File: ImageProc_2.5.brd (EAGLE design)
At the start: 49.8 x 23.2 mm, 117 parts, among them IC1 XC61GC3002HR-G, IC10 AT45DB642D-CNU, IC2 MIC5335-SPYMT, IC3 MIC5335-JGYMT, IC4 DSPIC33FJ128MC706A, IC5 AT86RF233-ZU, IC6 LTC6088, IC7 DRV8833RTY, IC8 DRV8833RTY, IC9 MPU-6000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

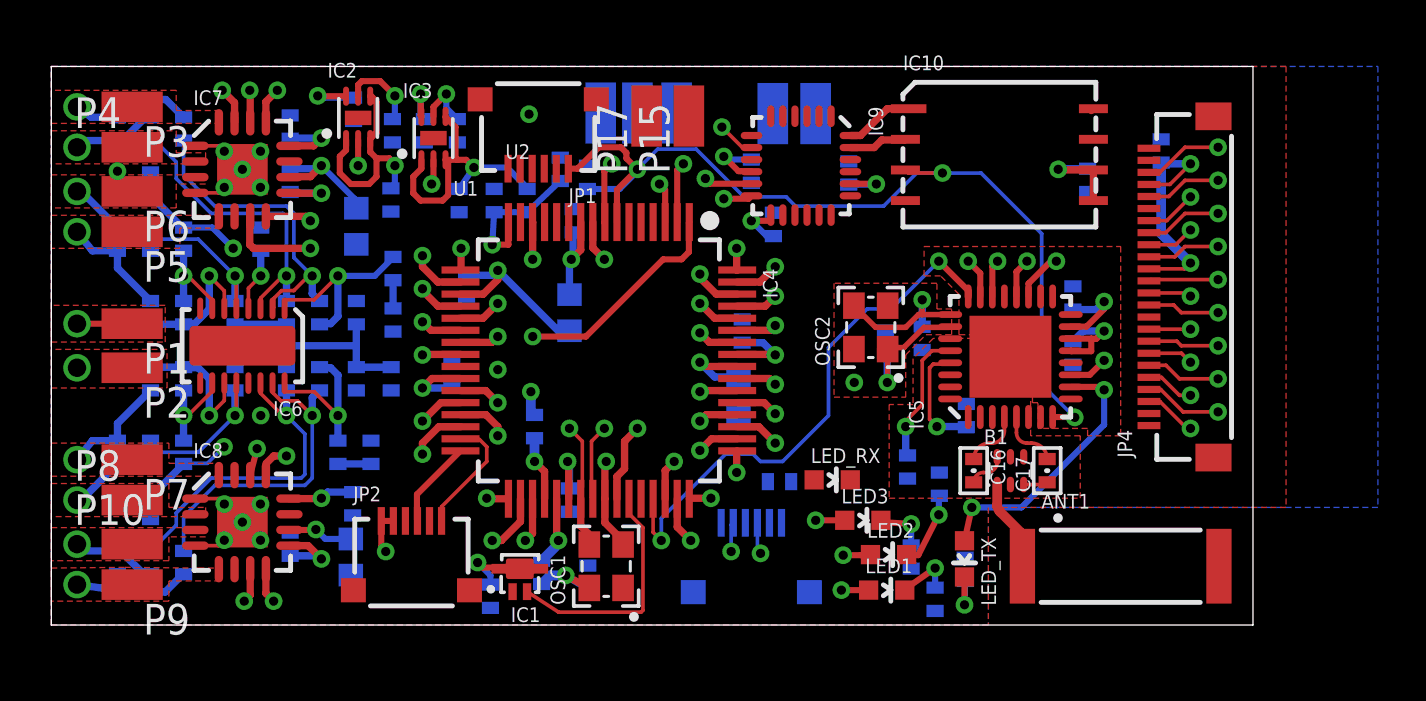
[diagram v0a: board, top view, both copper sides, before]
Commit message: ran DRC, fixed DRC issues for top and ground.
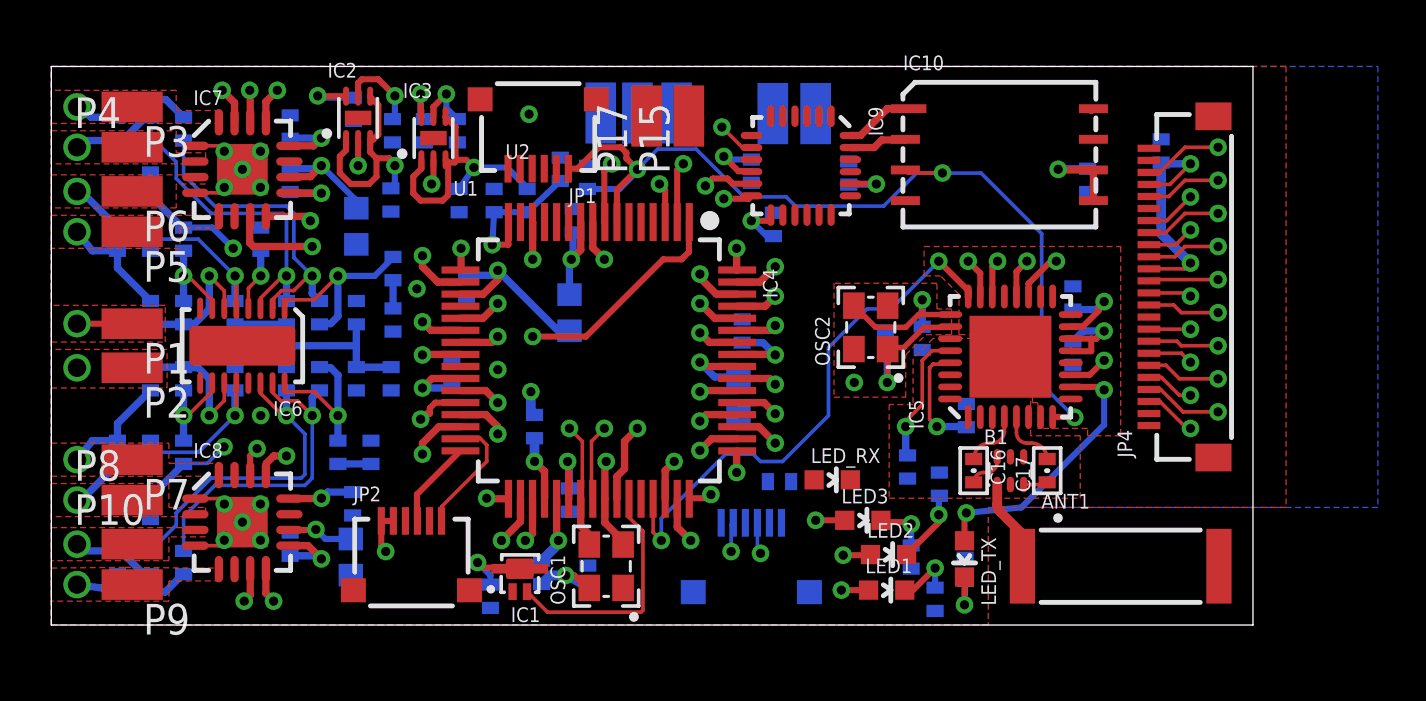
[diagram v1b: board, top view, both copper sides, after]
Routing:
- net CAM_HREF: track 39.2 -> 35.6 mm
- net SCL1: track 57.9 -> 55.7 mm
- net GND: track 14.9 -> 13.0 mm, vias 20 -> 19
- net SDI1: track 31.6 -> 31.1 mm

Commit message: Fixed rest of the initial DRC errors.
Down to 24 air wires.

Having to be creative for the pads.
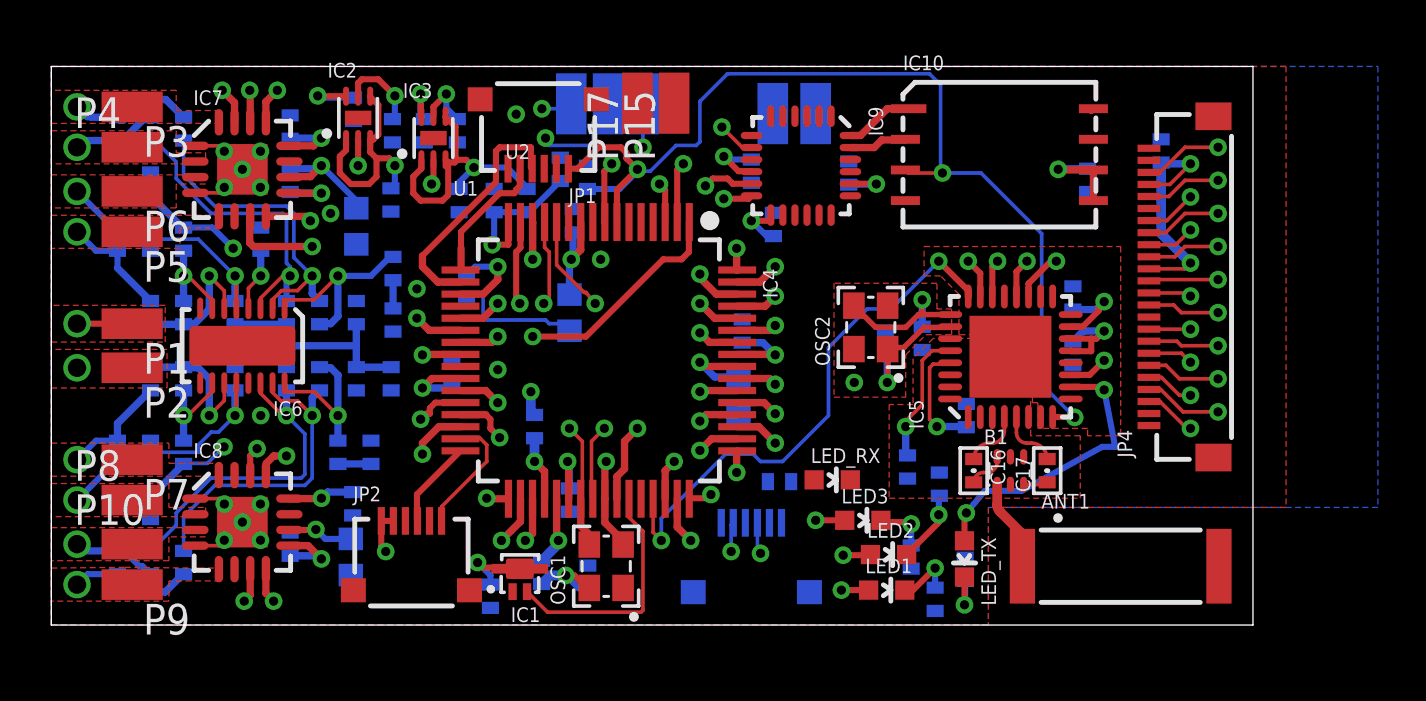
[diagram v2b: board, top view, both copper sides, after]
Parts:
- moved P13 1.42 mm to (24.6, 21.6)
- moved P11 1.28 mm to (21.6, 21.6)
- moved P12 1.28 mm to (23.1, 21.6)
- moved P15 0.81 mm to (25.8, 21.6)
- moved P17 0.66 mm to (24.3, 21.6)
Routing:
- net MOTOR_C_IN2: track 2.41 -> 41.7 mm, vias 2 -> 3
- net AN3/INDX/RB3: track 0.00 -> 21.3 mm, vias 0 -> 2
- net MOTOR_B_IN1: track 5.60 -> 26.3 mm
- net AN1/RB1: track 0.00 -> 17.8 mm, vias 0 -> 2
- net AN4/QEA/IC7/RB4: track 0.00 -> 14.8 mm, vias 0 -> 2
- net MOTOR_C_IN1: track 25.1 -> 33.4 mm
- net PGD: track 2.30 -> 10.3 mm, vias 1 -> 0
- net GN_LED: track 30.3 -> 23.9 mm
- net !RESET: track 39.2 -> 43.9 mm
- net PGC: track 0.91 -> 5.58 mm, vias 1 -> 0
- net MOTOR_C_BEMF: track 19.2 -> 23.8 mm
- net RD_LED: track 21.9 -> 18.4 mm
- net N$21: track 7.56 -> 10.2 mm
- net YW_LED: track 22.6 -> 20.7 mm
- net GND: track 13.0 -> 11.2 mm
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
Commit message: 17 airwires left.
did most of the wiring of the pads && the relocating of various ground and power layer wires to compensate.
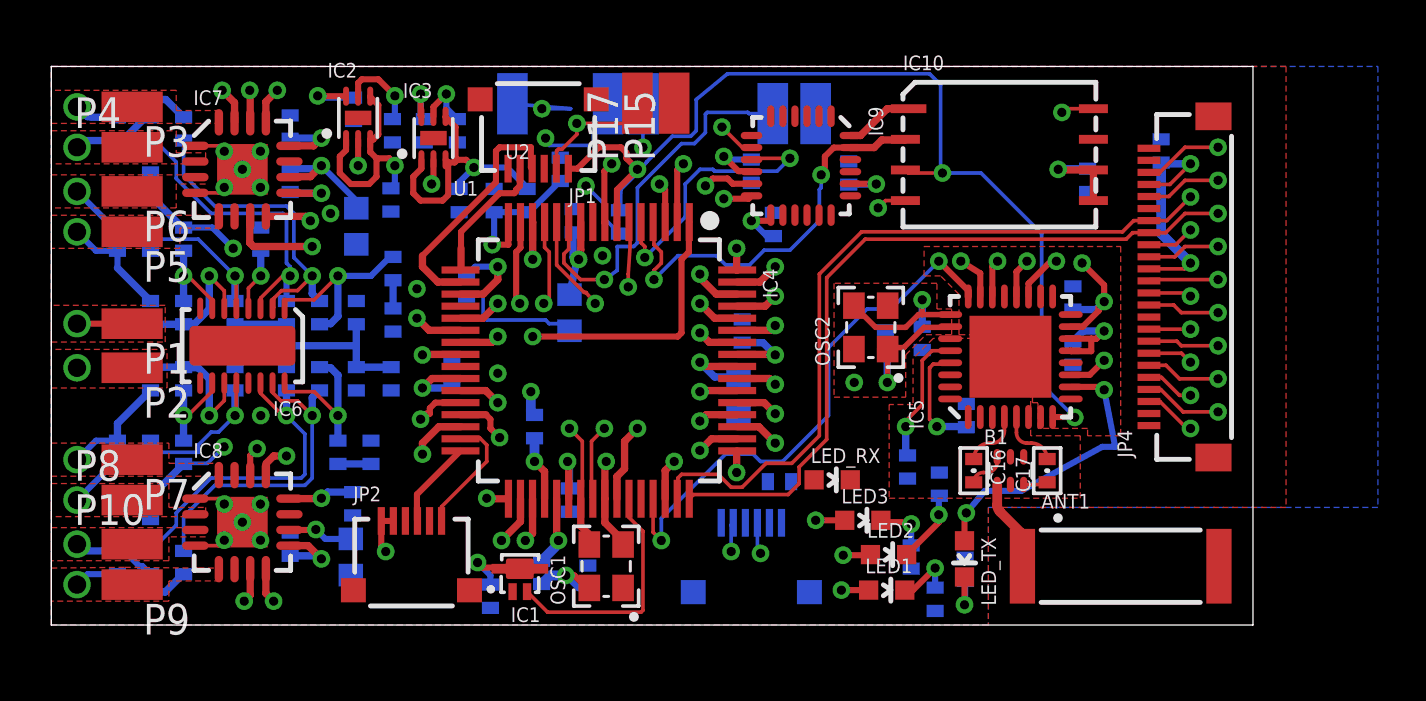
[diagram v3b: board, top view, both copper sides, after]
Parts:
- moved P11 2.44 mm to (19.1, 21.6)
- moved R3 2.28 mm to (23.6, 16.7), turned to 270 degrees
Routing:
- net CAM_VSYNC: track 4.09 -> 31.3 mm, vias 2 -> 1
- net CAM_PWDN: track 4.17 -> 31.2 mm, vias 2 -> 1
- net SDI2: track 0.12 -> 25.2 mm, vias 0 -> 3
- net AN5/QEB/IC8/RB5: track 0.00 -> 15.9 mm, vias 0 -> 1
- net SCK2: track 2.42 -> 17.2 mm, vias 0 -> 2
- net !SS2_1: track 2.59 -> 16.1 mm, vias 1 -> 2
- net 3.3V: track 46.8 -> 59.5 mm, vias 13 -> 15
- net !SS1: track 23.0 -> 27.9 mm
- net MOTOR_B_IN2: track 21.8 -> 26.4 mm
- net MOTOR_B_IN1: track 26.3 -> 30.7 mm
- net MOTOR_A_IN2: track 29.0 -> 33.2 mm
- net MOTOR_A_IN1: track 34.3 -> 38.2 mm
- net SDO2: track 2.88 -> 5.59 mm, vias 0 -> 1
- net AN1/RB1: track 17.8 -> 20.0 mm
- net MOTOR_C_IN1: track 33.4 -> 35.2 mm
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
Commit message: 3 airwires left….
begun fixing the airwires in the motor controller section
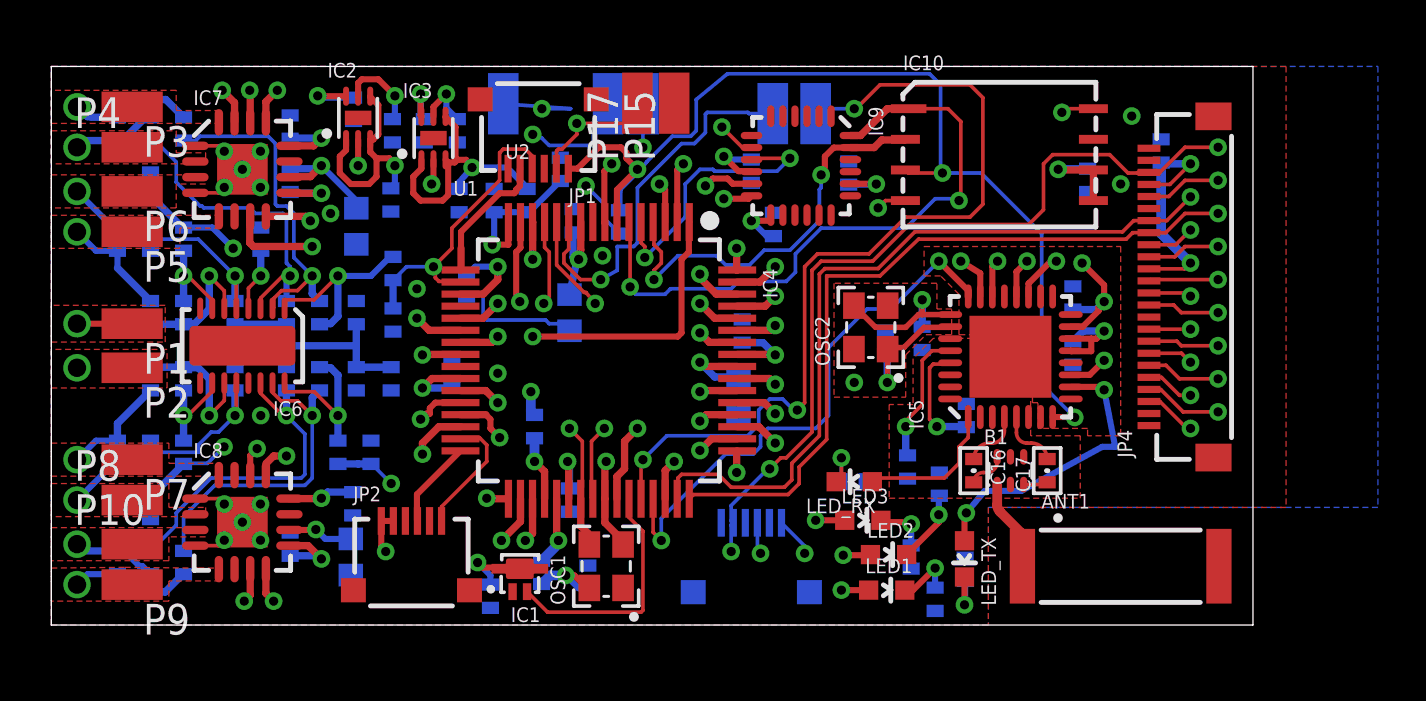
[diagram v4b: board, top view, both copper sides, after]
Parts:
- moved R7 3.05 mm to (33.2, 5.94)
- moved LED_RX 0.92 mm to (33.3, 5.94), turned to 90 degrees
- moved P11 0.38 mm to (18.7, 21.6)
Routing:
- net IC3/INT3/RD10: track 0.00 -> 36.2 mm, vias 0 -> 3
- net SDA1: track 15.0 -> 44.4 mm, vias 3 -> 4
- net SDO2: track 5.59 -> 27.2 mm, vias 1 -> 2
- net MOTOR_D_BEMF: track 2.96 -> 10.5 mm, vias 1 -> 2
- net N$13: track 0.00 -> 5.99 mm
- net MOTOR_A_BEMF: track 2.97 -> 8.17 mm, vias 1 -> 2
- net MOTOR_A_IN1: track 38.2 -> 36.0 mm
- net N$11: track 0.00 -> 2.07 mm, vias 0 -> 1
- net 3.3V: track 59.5 -> 61.2 mm, vias 15 -> 16
- net MOTOR_A_IN2: track 33.2 -> 31.8 mm
- net PGD: track 10.3 -> 9.48 mm
- net N$30: track 13.2 -> 13.9 mm
- net GND: vias 19 -> 21
